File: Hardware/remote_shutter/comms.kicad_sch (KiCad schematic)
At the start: 11 parts, among them J5 USB_C_Receptacle_USB2.0, Q3 BC847BDW1, U3 CP2102N-Axx-xQFN24

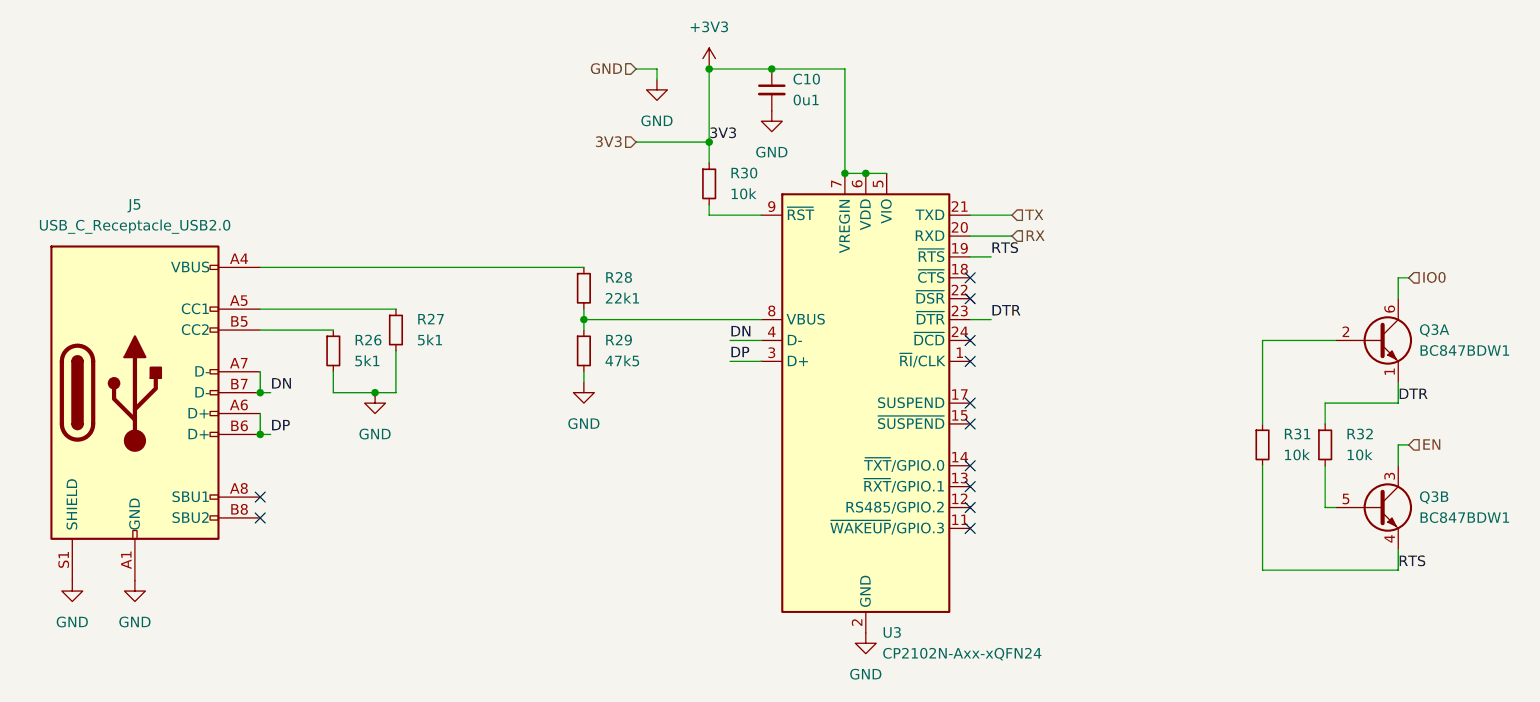
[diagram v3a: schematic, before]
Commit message: Added LiIon charge circuit
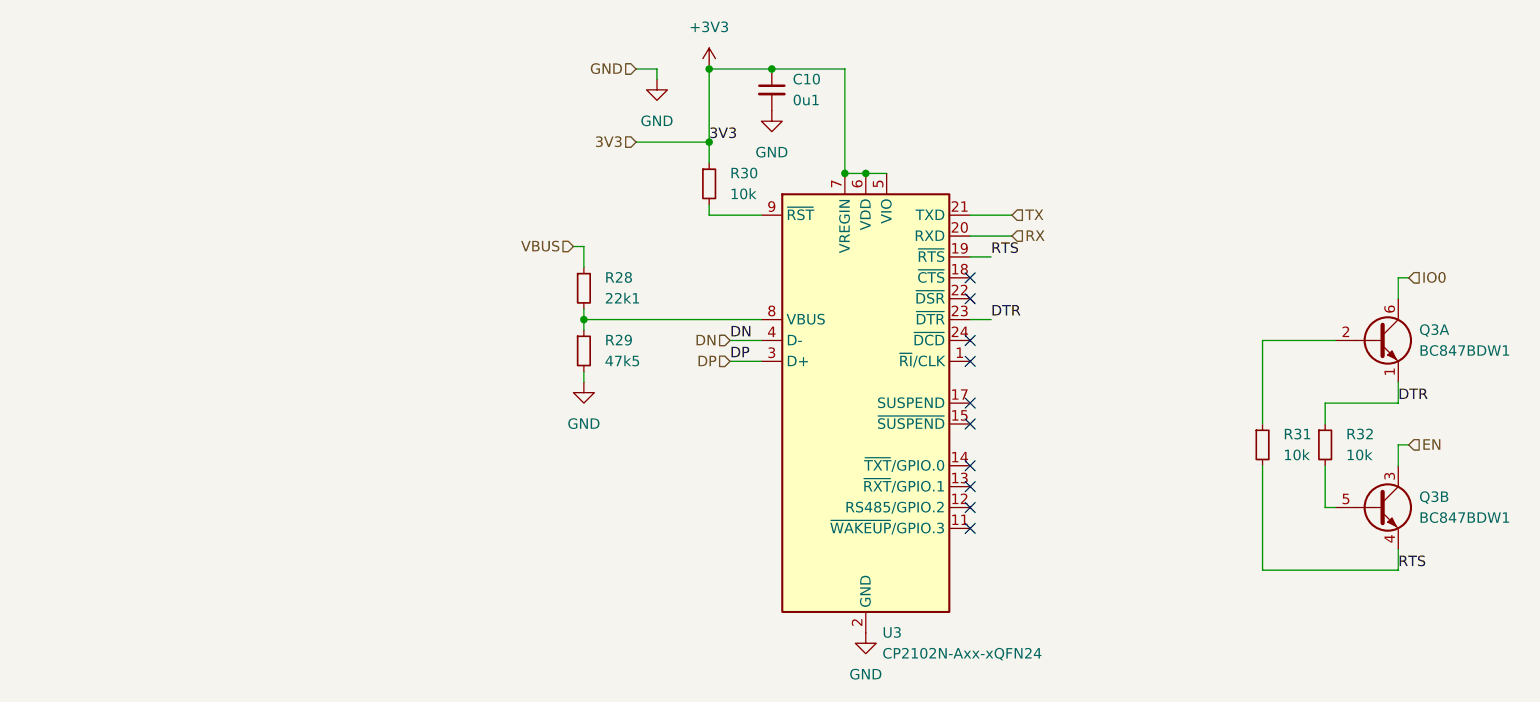
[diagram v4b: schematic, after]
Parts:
- removed J5: USB_C_Receptacle_USB2.0, symbol Connector:USB_C_Receptacle_USB2.0
- removed R26, R27: 5k1, Resistor_SMD:R_0603_1608Metric_Pad0.98x0.95mm_HandSolder, symbol Device:R_Small
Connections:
- net VBUS: now reaches R28.1
- no-connect marks 12 -> 10
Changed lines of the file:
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@@
   (junction (at 139.7 58.42) (diameter 0) (color 0 0 0 0)
   )
-  (junction (at 68.58 90.17) (diameter 0) (color 0 0 0 0)
-  )
   (junction (at 142.24 58.42) (diameter 0) (color 0 0 0 0)
   )
@@
   (junction (at 123.19 54.61) (diameter 0) (color 0 0 0 0)
   )
-  (junction (at 68.58 85.09) (diameter 0) (color 0 0 0 0)
-  )
   (junction (at 123.19 45.72) (diameter 0) (color 0 0 0 0)
   )
   (junction (at 107.95 76.2) (diameter 0) (color 0 0 0 0)
   )
-  (junction (at 82.55 85.09) (diameter 0) (color 0 0 0 0)
-  )
-  (no_connect (at 68.58 100.33))
-  (no_connect (at 68.58 97.79))
   (no_connect (at 154.94 81.28))
   (no_connect (at 154.94 78.74))
@@
   (no_connect (at 154.94 99.06))
   (no_connect (at 154.94 101.6))
-  (wire (pts (xy 68.58 82.55) (xy 68.58 85.09))
-    (stroke (width 0) (type default) (color 0 0 0 0))
-  )
   (wire (pts (xy 208.28 91.44) (xy 207.01 91.44))
     (stroke (width 0) (type default) (color 0 0 0 0))
@@
     (stroke (width 0) (type default) (color 0 0 0 0))
   )
-  (wire (pts (xy 68.58 77.47) (xy 77.47 77.47))
-    (stroke (width 0) (type default) (color 0 0 0 0))
-  )
   (wire (pts (xy 199.39 78.74) (xy 190.5 78.74))
     (stroke (width 0) (type default) (color 0 0 0 0))
@@
     (stroke (width 0) (type default) (color 0 0 0 0))
   )
+  (wire (pts (xy 107.95 69.85) (xy 107.95 67.31))
+    (stroke (width 0) (type default) (color 0 0 0 0))
+  )
   (wire (pts (xy 125.73 78.74) (xy 129.54 78.74))
     (stroke (width 0) (type default) (color 0 0 0 0))
@@
     (stroke (width 0) (type default) (color 0 0 0 0))
   )
-  (wire (pts (xy 68.58 85.09) (xy 69.85 85.09))
-    (stroke (width 0) (type default) (color 0 0 0 0))
-  )
   (wire (pts (xy 125.73 81.28) (xy 129.54 81.28))
     (stroke (width 0) (type default) (color 0 0 0 0))
@@
     (stroke (width 0) (type default) (color 0 0 0 0))
   )
-  (wire (pts (xy 68.58 87.63) (xy 68.58 90.17))
-    (stroke (width 0) (type default) (color 0 0 0 0))
-  )
   (wire (pts (xy 116.84 45.72) (xy 116.84 46.99))
     (stroke (width 0) (type default) (color 0 0 0 0))
@@
     (stroke (width 0) (type default) (color 0 0 0 0))
   )
-  (wire (pts (xy 77.47 82.55) (xy 77.47 85.09))
-    (stroke (width 0) (type default) (color 0 0 0 0))
-  )
   (wire (pts (xy 190.5 106.68) (xy 207.01 106.68))
     (stroke (width 0) (type default) (color 0 0 0 0))
   )
-  (wire (pts (xy 68.58 90.17) (xy 69.85 90.17))
-    (stroke (width 0) (type default) (color 0 0 0 0))
-  )
-  (wire (pts (xy 68.58 69.85) (xy 107.95 69.85))
-    (stroke (width 0) (type default) (color 0 0 0 0))
-  )
   (wire (pts (xy 198.12 99.06) (xy 199.39 99.06))
     (stroke (width 0) (type default) (color 0 0 0 0))
@@
     (stroke (width 0) (type default) (color 0 0 0 0))
   )
-  (wire (pts (xy 85.09 85.09) (xy 82.55 85.09))
-    (stroke (width 0) (type default) (color 0 0 0 0))
-  )
   (wire (pts (xy 130.81 45.72) (xy 139.7 45.72))
     (stroke (width 0) (type default) (color 0 0 0 0))
@@
     (stroke (width 0) (type default) (color 0 0 0 0))
   )
-  (wire (pts (xy 77.47 85.09) (xy 82.55 85.09))
-    (stroke (width 0) (type default) (color 0 0 0 0))
-  )
-  (wire (pts (xy 85.09 80.01) (xy 85.09 85.09))
-    (stroke (width 0) (type default) (color 0 0 0 0))
-  )
   (wire (pts (xy 207.01 91.44) (xy 207.01 93.98))
     (stroke (width 0) (type default) (color 0 0 0 0))
   )
-  (wire (pts (xy 68.58 74.93) (xy 85.09 74.93))
-    (stroke (width 0) (type default) (color 0 0 0 0))
-  )
   (wire (pts (xy 107.95 74.93) (xy 107.95 76.2))
     (stroke (width 0) (type default) (color 0 0 0 0))
@@
     (stroke (width 0) (type default) (color 0 0 0 0))
   )
+  (wire (pts (xy 107.95 67.31) (xy 106.68 67.31))
+    (stroke (width 0) (type default) (color 0 0 0 0))
+  )
   (label "RTS" (at 207.01 106.68 0)
     (effects (font (size 1.27 1.27)) (justify left bottom))
@@
   )
   (label "DTR" (at 207.01 86.36 0)
-    (effects (font (size 1.27 1.27)) (justify left bottom))
-  )
-  (label "DN" (at 69.85 85.09 0)
-    (effects (font (size 1.27 1.27)) (justify left bottom))
-  )
-  (label "DP" (at 69.85 90.17 0)
     (effects (font (size 1.27 1.27)) (justify left bottom))
   )
@@
   (hierarchical_label "IO0" (shape input) (at 208.28 71.12 0)
     (effects (font (size 1.27 1.27)) (justify left))
+  )
+  (hierarchical_label "VBUS" (shape input) (at 106.68 67.31 180)
+    (effects (font (size 1.27 1.27)) (justify right))
+  )
+  (hierarchical_label "DN" (shape input) (at 125.73 78.74 180)
+    (effects (font (size 1.27 1.27)) (justify right))
+  )
+  (hierarchical_label "DP" (shape input) (at 125.73 81.28 180)
+    (effects (font (size 1.27 1.27)) (justify right))
   )
   (hierarchical_label "3V3" (shape input) (at 114.3 54.61 180)
@@
   (symbol (lib_id "power:+3V3") (at 123.19 45.72 0) (unit 1)
     (in_bom yes) (on_board yes) (fields_autoplaced)
-    (property "Reference" "#PWR?" (id 0) (at 123.19 49.53 0)
+    (property "Reference" "#PWR0127" (id 0) (at 123.19 49.53 0)
       (effects (font (size 1.27 1.27)) hide)
     )
@@
     (pin "1")
   )
-  (symbol (lib_id "power:GND") (at 45.72 107.95 0) (unit 1)
-    (in_bom yes) (on_board yes) (fields_autoplaced)
-    (property "Reference" "#PWR0123" (id 0) (at 45.72 114.3 0)
-      (effects (font (size 1.27 1.27)) hide)
-    )
-    (property "Value" "GND" (id 1) (at 45.72 113.03 0))
-    (property "Footprint" "" (id 2) (at 45.72 107.95 0)
-      (effects (font (size 1.27 1.27)) hide)
-    )
-    (property "Datasheet" "" (id 3) (at 45.72 107.95 0)
-      (effects (font (size 1.27 1.27)) hide)
-    )
-    (pin "1")
-  )
   (symbol (lib_id "power:GND") (at 107.95 83.82 0) (unit 1)
     (in_bom yes) (on_board yes) (fields_autoplaced)
@@
     (pin "1")
     (pin "2")
-  )
-  (symbol (lib_id "Connector:USB_C_Receptacle_USB2.0") (at 53.34 85.09 0) (unit 1)
-    (in_bom yes) (on_board yes) (fields_autoplaced)
-    (property "Reference" "J5" (id 0) (at 53.34 62.23 0))
-    (property "Value" "USB_C_Receptacle_USB2.0" (id 1) (at 53.34 64.77 0))
-    (property "Footprint" "" (id 2) (at 57.15 85.09 0)
-      (effects (font (size 1.27 1.27)) hide)
-    )
-    (property "Datasheet" "https://www.usb.org/sites/default/files/documents/usb_type-c.zip" (id 3) (at 57.15 85.09 0)
-      (effects (font (size 1.27 1.27)) hide)
-    )
-    (pin "A1")
-    (pin "A12")
-    (pin "A4")
-    (pin "A5")
-    (pin "A6")
-    (pin "A7")
-    (pin "A8")
-    (pin "A9")
-    (pin "B1")
-    (pin "B12")
-    (pin "B4")
-    (pin "B5")
-    (pin "B6")
-    (pin "B7")
-    (pin "B8")
-    (pin "B9")
-    (pin "S1")
   )
   (symbol (lib_id "power:GND") (at 116.84 46.99 0) (unit 1)
@@
     (pin "2")
   )
-  (symbol (lib_id "power:GND") (at 53.34 107.95 0) (unit 1)
-    (in_bom yes) (on_board yes) (fields_autoplaced)
-    (property "Reference" "#PWR0122" (id 0) (at 53.34 114.3 0)
-      (effects (font (size 1.27 1.27)) hide)
-    )
-    (property "Value" "GND" (id 1) (at 53.34 113.03 0))
-    (property "Footprint" "" (id 2) (at 53.34 107.95 0)
-      (effects (font (size 1.27 1.27)) hide)
-    )
-    (property "Datasheet" "" (id 3) (at 53.34 107.95 0)
-      (effects (font (size 1.27 1.27)) hide)
-    )
-    (pin "1")
-  )
-  (symbol (lib_id "Device:R_Small") (at 85.09 77.47 0) (unit 1)
-    (in_bom yes) (on_board yes) (fields_autoplaced)
-    (property "Reference" "R27" (id 0) (at 87.63 76.1999 0)
-      (effects (font (size 1.27 1.27)) (justify left))
-    )
-    (property "Value" "5k1" (id 1) (at 87.63 78.7399 0)
-      (effects (font (size 1.27 1.27)) (justify left))
-    )
-    (property "Footprint" "Resistor_SMD:R_0603_1608Metric_Pad0.98x0.95mm_HandSolder" (id 2) (at 85.09 77.47 0)
-      (effects (font (size 1.27 1.27)) hide)
-    )
-    (property "Datasheet" "~" (id 3) (at 85.09 77.47 0)
-      (effects (font (size 1.27 1.27)) hide)
-    )
-    (pin "1")
-    (pin "2")
-  )
   (symbol (lib_id "Device:R_Small") (at 190.5 91.44 0) (unit 1)
     (in_bom yes) (on_board yes) (fields_autoplaced)
@@
       (effects (font (size 1.27 1.27)) hide)
     )
-    (pin "1")
-    (pin "2")
-  )
-  (symbol (lib_id "power:GND") (at 82.55 85.09 0) (unit 1)
-    (in_bom yes) (on_board yes) (fields_autoplaced)
-    (property "Reference" "#PWR0121" (id 0) (at 82.55 91.44 0)
-      (effects (font (size 1.27 1.27)) hide)
-    )
-    (property "Value" "GND" (id 1) (at 82.55 90.17 0))
-    (property "Footprint" "" (id 2) (at 82.55 85.09 0)
-      (effects (font (size 1.27 1.27)) hide)
-    )
-    (property "Datasheet" "" (id 3) (at 82.55 85.09 0)
-      (effects (font (size 1.27 1.27)) hide)
-    )
-    (pin "1")
-  )
-  (symbol (lib_id "Device:R_Small") (at 77.47 80.01 0) (unit 1)
-    (in_bom yes) (on_board yes) (fields_autoplaced)
-    (property "Reference" "R26" (id 0) (at 80.01 78.7399 0)
-      (effects (font (size 1.27 1.27)) (justify left))
-    )
-    (property "Value" "5k1" (id 1) (at 80.01 81.2799 0)
-      (effects (font (size 1.27 1.27)) (justify left))
-    )
-    (property "Footprint" "Resistor_SMD:R_0603_1608Metric_Pad0.98x0.95mm_HandSolder" (id 2) (at 77.47 80.01 0)
-      (effects (font (size 1.27 1.27)) hide)
-    )
-    (property "Datasheet" "~" (id 3) (at 77.47 80.01 0)
-      (effects (font (size 1.27 1.27)) hide)
-    )
